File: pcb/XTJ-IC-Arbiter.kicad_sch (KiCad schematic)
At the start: 33 parts, among them J3 DTM13-12PA-R008, SW1 SW_DIP_x01, SW2 SW_DIP_x01, U1 LM2672N-5.0, U3 Teensy4.0, U4 MCP2562-H-P, U5 SP723ABG

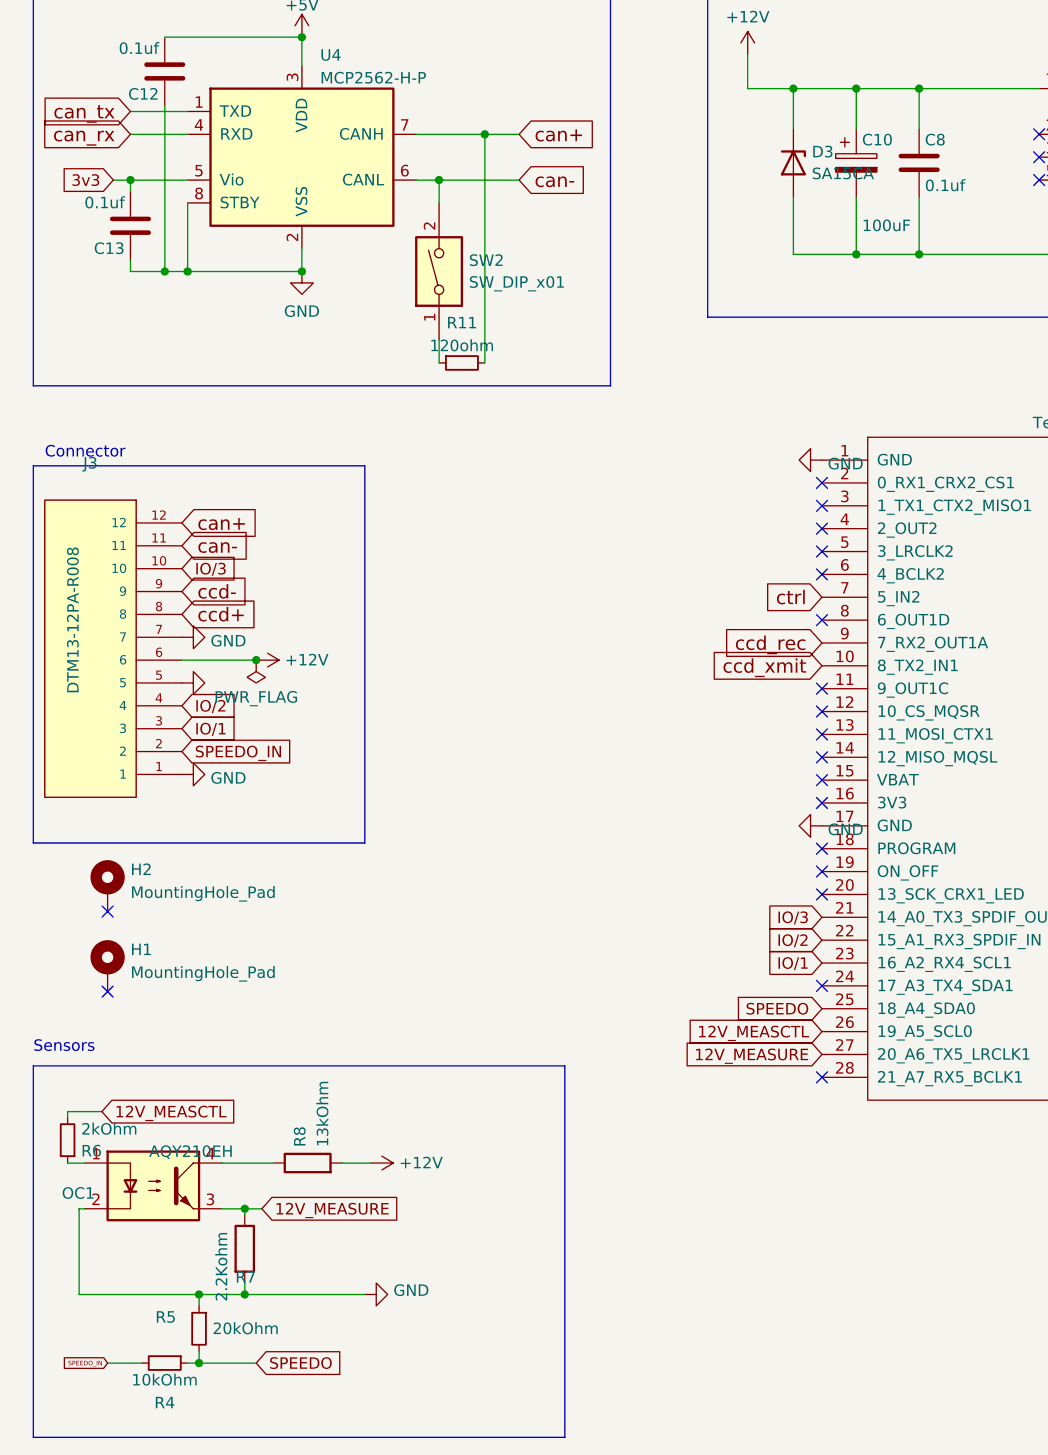
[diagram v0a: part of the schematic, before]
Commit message: Recalculate the 12v measure voltage dividers, and add a zener to limit to 3.3v
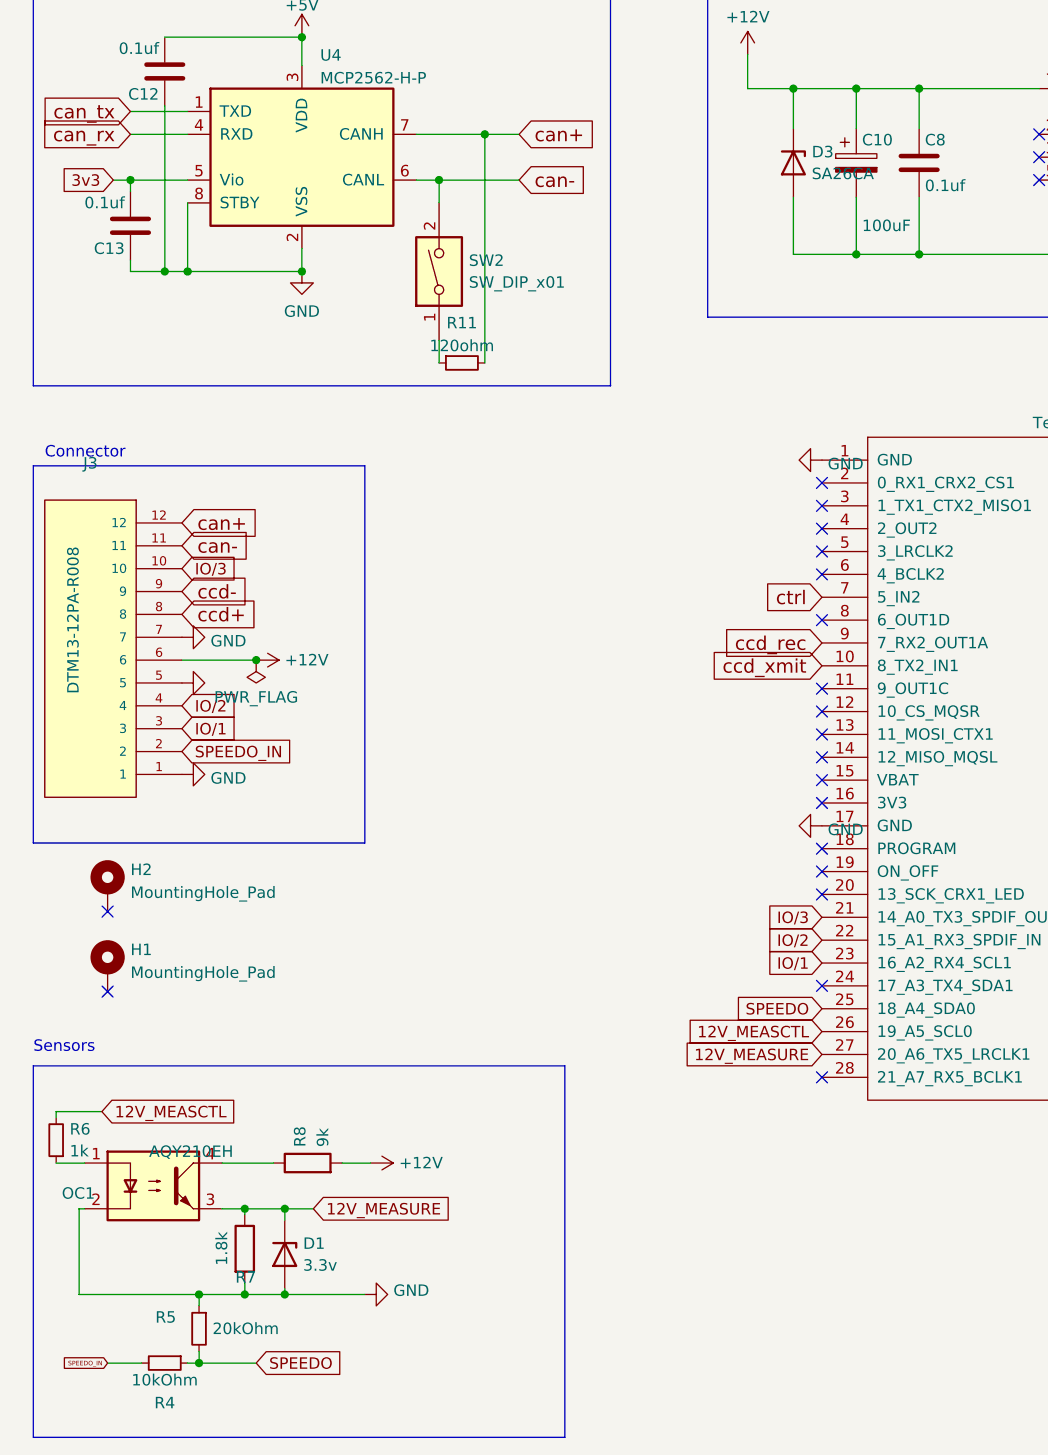
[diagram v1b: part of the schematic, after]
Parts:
- added D1: 3.3v, Diode_THT:D_DO-35_SOD27_P7.62mm_Horizontal, symbol Device:D_Zener
- D3: value SA15CA -> SA26CA
- R6: value 2kOhm -> 1k
- R7: value 2.2Kohm -> 1.8k
- R8: value 13kOhm -> 9k
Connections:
- net 12V_MEASURE: now also D1.1 (K)
- net GND: now also D1.2 (A)
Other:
- moved on the sheet: R6
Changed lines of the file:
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@@
   (junction (at 109.22 54.61) (diameter 0) (color 0 0 0 0)
   )
+  (junction (at 45.72 160.655) (diameter 0) (color 0 0 0 0)
+  )
   (junction (at 28.575 46.355) (diameter 0) (color 0 0 0 0)
   )
@@
   )
   (junction (at 62.865 46.355) (diameter 0) (color 0 0 0 0)
+  )
+  (junction (at 45.72 170.18) (diameter 0) (color 0 0 0 0)
   )
   (junction (at 249.555 34.29) (diameter 0) (color 0 0 0 0)
@@
     (stroke (width 0) (type default))
   )
+  (wire (pts (xy 45.72 169.545) (xy 45.72 170.18))
+    (stroke (width 0) (type default))
+  )
   (wire (pts (xy 161.29 135.89) (xy 167.005 135.89))
     (stroke (width 0) (type default))
@@
     (stroke (width 0) (type default))
   )
-  (wire (pts (xy 25.4 149.86) (xy 21.59 149.86))
+  (wire (pts (xy 25.4 149.86) (xy 20.32 149.86))
     (stroke (width 0) (type default))
   )
@@
     (stroke (width 0) (type default))
   )
-  (wire (pts (xy 21.59 155.575) (xy 23.495 155.575))
+  (wire (pts (xy 20.32 155.575) (xy 23.495 155.575))
     (stroke (width 0) (type default))
   )
@@
     (stroke (width 0) (type default))
   )
+  (wire (pts (xy 41.275 160.655) (xy 45.72 160.655))
+    (stroke (width 0) (type default))
+  )
   (wire (pts (xy 169.545 46.355) (xy 173.355 46.355))
     (stroke (width 0) (type default))
@@
     (stroke (width 0) (type default))
   )
-  (wire (pts (xy 43.18 160.655) (xy 41.275 160.655))
-    (stroke (width 0) (type default))
-  )
   (wire (pts (xy 207.645 34.29) (xy 207.645 57.785))
     (stroke (width 0) (type default))
@@
     (stroke (width 0) (type default))
   )
+  (wire (pts (xy 45.72 160.655) (xy 45.72 161.925))
+    (stroke (width 0) (type default))
+  )
   (wire (pts (xy 144.78 54.61) (xy 160.02 54.61))
     (stroke (width 0) (type default))
@@
     (stroke (width 0) (type default))
   )
+  (wire (pts (xy 45.72 170.18) (xy 54.61 170.18))
+    (stroke (width 0) (type default))
+  )
   (wire (pts (xy 109.22 36.195) (xy 116.205 36.195))
     (stroke (width 0) (type default))
   )
-  (wire (pts (xy 21.59 149.86) (xy 21.59 150.495))
+  (wire (pts (xy 20.32 149.86) (xy 20.32 150.495))
     (stroke (width 0) (type default))
   )
@@
     (stroke (width 0) (type default))
   )
+  (wire (pts (xy 45.72 160.655) (xy 48.895 160.655))
+    (stroke (width 0) (type default))
+  )
   (polyline (pts (xy 81.915 24.13) (xy 81.915 69.215))
     (stroke (width 0) (type default))
@@
     (stroke (width 0) (type default))
   )
-  (wire (pts (xy 41.275 170.18) (xy 54.61 170.18))
+  (wire (pts (xy 41.275 170.18) (xy 45.72 170.18))
     (stroke (width 0) (type default))
   )
@@
     )
   )
-  (global_label "12V_MEASURE" (shape input) (at 43.18 160.655 0) (fields_autoplaced)
+  (global_label "12V_MEASURE" (shape input) (at 48.895 160.655 0) (fields_autoplaced)
     (effects (font (size 1.27 1.27)) (justify left))
-    (property "Intersheetrefs" "${INTERSHEET_REFS}" (at 58.7164 160.7344 0)
+    (property "Intersheetrefs" "${INTERSHEET_REFS}" (at 64.4314 160.7344 0)
       (effects (font (size 1.27 1.27)) (justify left) hide)
     )
@@
       (effects (font (size 1.27 1.27)) (justify left))
     )
-    (property "Value" "13kOhm" (at 49.9622 153.797 0)
+    (property "Value" "9k" (at 49.9622 153.797 0)
       (effects (font (size 1.27 1.27)) (justify left))
     )
@@
     )
   )
-  (symbol (lib_id "Device:R_Small") (at 21.59 153.035 180) (unit 1)
-    (in_bom yes) (on_board yes) (dnp no) (fields_autoplaced)
-    (property "Reference" "R6" (at 23.0886 154.2471 0)
+  (symbol (lib_id "Device:R_Small") (at 20.32 153.035 180) (unit 1)
+    (in_bom yes) (on_board yes) (dnp no) (fields_autoplaced)
+    (property "Reference" "R6" (at 21.8186 151.8229 0)
       (effects (font (size 1.27 1.27)) (justify right))
     )
-    (property "Value" "2kOhm" (at 23.0886 151.8229 0)
+    (property "Value" "1k" (at 21.8186 154.2471 0)
       (effects (font (size 1.27 1.27)) (justify right))
     )
-    (property "Footprint" "Resistor_THT:R_Axial_DIN0207_L6.3mm_D2.5mm_P7.62mm_Horizontal" (at 21.59 153.035 0)
-      (effects (font (size 1.27 1.27)) hide)
-    )
-    (property "Datasheet" "~" (at 21.59 153.035 0)
+    (property "Footprint" "Resistor_THT:R_Axial_DIN0207_L6.3mm_D2.5mm_P7.62mm_Horizontal" (at 20.32 153.035 0)
+      (effects (font (size 1.27 1.27)) hide)
+    )
+    (property "Datasheet" "~" (at 20.32 153.035 0)
       (effects (font (size 1.27 1.27)) hide)
     )
@@
       (effects (font (size 1.27 1.27)) (justify right))
     )
-    (property "Value" "2.2Kohm" (at 38.735 163.195 90)
+    (property "Value" "1.8k" (at 38.735 163.195 90)
       (effects (font (size 1.27 1.27)) (justify right))
     )
@@
       (effects (font (size 1.27 1.27)) (justify left))
     )
-    (property "Value" "SA15CA" (at 104.267 45.6621 90)
+    (property "Value" "SA26CA" (at 104.267 45.6621 90)
       (effects (font (size 1.27 1.27)) (justify left))
     )
@@
         )
       )
+    )
+  )
+  (symbol (lib_id "Device:D_Zener") (at 45.72 165.735 270) (unit 1)
+    (in_bom yes) (on_board yes) (dnp no) (fields_autoplaced)
+    (property "Reference" "D1" (at 47.752 164.5229 90)
+      (effects (font (size 1.27 1.27)) (justify left))
+    )
+    (property "Value" "3.3v" (at 47.752 166.9471 90)
+      (effects (font (size 1.27 1.27)) (justify left))
+    )
+    (property "Footprint" "Diode_THT:D_DO-35_SOD27_P7.62mm_Horizontal" (at 45.72 165.735 0)
+      (effects (font (size 1.27 1.27)) hide)
+    )
+    (property "Datasheet" "~" (at 45.72 165.735 0)
+      (effects (font (size 1.27 1.27)) hide)
+    )
+    (pin "2")
+    (pin "1")
+    (instances
+      (project "XTJ-IC-Arbiter"
+        (path "/30a59342-dbf1-42d2-913c-7e79095896d9"
+          (reference "D1") (unit 1)
+        )
+      )

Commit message: ugly but functional
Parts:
- removed C2: 0.1uf, Capacitor_THT:C_Disc_D3.8mm_W2.6mm_P2.50mm, symbol Device:C
- added D2: 1N4001GH, Diode_THT:D_DO-41_SOD81_P7.62mm_Horizontal, symbol Device:D
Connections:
- net ctrl is gone; now on net ccd_rec: U2.13 (CTRL), U3.7 (5_IN2)
- net +5V: now also D2.2 (A)
- net 12V_MEASCTL: now also U3.27 (20_A6_TX5_LRCLK1); no longer U3.26 (19_A5_SCL0)
- net 12V_MEASURE: now also U3.26 (19_A5_SCL0); no longer U3.27 (20_A6_TX5_LRCLK1)
- net GND: no longer J3.5
- net IO/1: now also U5.7 (IN); no longer U5.5 (IN_4)
- net IO/3: now also U5.5 (IN_4); no longer U5.7 (IN)
- net can+: now also J3.9; no longer J3.12
- net can-: now also J3.8; no longer J3.11
- net ccd+: now also J3.11, U5.2 (IN_3); no longer J3.8, U5.1 (IN_2)
- net ccd-: now also J3.12, U5.1 (IN_2); no longer J3.9, U5.2 (IN_3)
- new net: D2.1 (K), J3.5

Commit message: less ugly
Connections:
- net 12V_MEASCTL: now also U3.24 (17_A3_TX4_SDA1); no longer U3.27 (20_A6_TX5_LRCLK1)
- net 12V_MEASURE: now also U3.25 (18_A4_SDA0); no longer U3.26 (19_A5_SCL0)
- net IO/1: now also J3.10, U3.21 (14_A0_TX3_SPDIF_OUT), U5.3 (IN_5); no longer J3.3, U3.23 (16_A2_RX4_SCL1), U5.7 (IN)
- net IO/2: now also J3.11, U3.23 (16_A2_RX4_SCL1), U5.2 (IN_3); no longer J3.4, U3.22 (15_A1_RX3_SPDIF_IN), U5.6 (IN_6)
- net IO/3: now also J3.12, U3.22 (15_A1_RX3_SPDIF_IN), U5.7 (IN); no longer J3.10, U3.21 (14_A0_TX3_SPDIF_OUT), U5.5 (IN_4)
- net SPEEDO: now also U3.26 (19_A5_SCL0), U5.1 (IN_2); no longer U3.25 (18_A4_SDA0), U5.3 (IN_5)
- net ccd+: now also J3.3, U5.6 (IN_6); no longer J3.11, U5.2 (IN_3)
- net ccd-: now also J3.4, U5.5 (IN_4); no longer J3.12, U5.1 (IN_2)
- net ccd_rec: now also U3.28 (21_A7_RX5_BCLK1); no longer U3.9 (7_RX2_OUT1A)
- net ccd_xmit: now also U3.27 (20_A6_TX5_LRCLK1); no longer U3.10 (8_TX2_IN1)

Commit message: polish, text
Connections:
- net IO/2: now also U3.22 (15_A1_RX3_SPDIF_IN), U5.7 (IN); no longer U3.23 (16_A2_RX4_SCL1), U5.2 (IN_3)
- net IO/3: now also U3.23 (16_A2_RX4_SCL1), U5.2 (IN_3); no longer U3.22 (15_A1_RX3_SPDIF_IN), U5.7 (IN)
- net ccd+: now also J3.4, U5.5 (IN_4); no longer J3.3, U5.6 (IN_6)
- net ccd-: now also J3.3, U5.6 (IN_6); no longer J3.4, U5.5 (IN_4)
- net 5VO: now reaches D2.1 (K), J3.5
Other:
- moved on the sheet: D2
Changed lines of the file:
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@@
+    (stroke (width 0) (type default))
+  )
+  (wire (pts (xy 45.085 102.235) (xy 34.29 102.235))
     (stroke (width 0) (type default))
   )
@@
     (stroke (width 0) (type default))
   )
-  (wire (pts (xy 41.91 102.235) (xy 42.545 102.235))
+  (wire (pts (xy 52.705 102.235) (xy 53.34 102.235))
     (stroke (width 0) (type default))
   )
@@
   )
   (text "Connector" (at 19.05 77.47 0)
+    (effects (font (size 1.27 1.27)) (justify left bottom))
+  )
+  (label "5VO" (at 45.085 102.235 0) (fields_autoplaced)
     (effects (font (size 1.27 1.27)) (justify left bottom))
   )
@@
     )
   )
-  (global_label "IO{slash}2" (shape input) (at 105.41 133.35 180) (fields_autoplaced)
+  (global_label "IO{slash}2" (shape input) (at 105.41 130.81 180) (fields_autoplaced)
     (effects (font (size 1.27 1.27)) (justify right))
-    (property "Intersheetrefs" "${INTERSHEET_REFS}" (at 98.5217 133.4294 0)
+    (property "Intersheetrefs" "${INTERSHEET_REFS}" (at 98.5217 130.8894 0)
       (effects (font (size 1.27 1.27)) (justify right) hide)
     )
@@
     )
   )
-  (global_label "ccd+" (shape input) (at 210.82 109.855 180) (fields_autoplaced)
+  (global_label "ccd+" (shape input) (at 210.82 104.775 180) (fields_autoplaced)
     (effects (font (size 1.524 1.524)) (justify right))
-    (property "Intersheetrefs" "${INTERSHEET_REFS}" (at 201.3599 109.855 0)
+    (property "Intersheetrefs" "${INTERSHEET_REFS}" (at 201.3599 104.775 0)
       (effects (font (size 1.27 1.27)) (justify right) hide)
     )
@@
     )
   )
-  (global_label "ccd+" (shape input) (at 34.29 107.315 0) (fields_autoplaced)
+  (global_label "ccd+" (shape input) (at 34.29 104.775 0) (fields_autoplaced)
     (effects (font (size 1.524 1.524)) (justify left))
-    (property "Intersheetrefs" "${INTERSHEET_REFS}" (at 256.54 212.725 0)
+    (property "Intersheetrefs" "${INTERSHEET_REFS}" (at 256.54 210.185 0)
       (effects (font (size 1.27 1.27)) hide)
     )
@@
     )
   )
-  (global_label "IO{slash}3" (shape input) (at 105.41 130.81 180) (fields_autoplaced)
+  (global_label "IO{slash}3" (shape input) (at 105.41 133.35 180) (fields_autoplaced)
     (effects (font (size 1.27 1.27)) (justify right))
-    (property "Intersheetrefs" "${INTERSHEET_REFS}" (at 98.5217 130.8894 0)
+    (property "Intersheetrefs" "${INTERSHEET_REFS}" (at 98.5217 133.4294 0)
       (effects (font (size 1.27 1.27)) (justify right) hide)
     )
@@
     )
   )
-  (global_label "IO{slash}3" (shape input) (at 210.82 112.395 180) (fields_autoplaced)
+  (global_label "IO{slash}3" (shape input) (at 210.82 102.235 180) (fields_autoplaced)
     (effects (font (size 1.27 1.27)) (justify right))
-    (property "Intersheetrefs" "${INTERSHEET_REFS}" (at 203.3595 112.395 0)
+    (property "Intersheetrefs" "${INTERSHEET_REFS}" (at 203.3595 102.235 0)
       (effects (font (size 1.27 1.27)) (justify right) hide)
     )
@@
     )
   )
-  (global_label "IO{slash}2" (shape input) (at 210.82 102.235 180) (fields_autoplaced)
+  (global_label "IO{slash}2" (shape input) (at 210.82 112.395 180) (fields_autoplaced)
     (effects (font (size 1.27 1.27)) (justify right))
-    (property "Intersheetrefs" "${INTERSHEET_REFS}" (at 203.3595 102.235 0)
+    (property "Intersheetrefs" "${INTERSHEET_REFS}" (at 203.3595 112.395 0)
       (effects (font (size 1.27 1.27)) (justify right) hide)
     )
@@
     )
   )
-  (global_label "ccd-" (shape input) (at 210.82 104.775 180) (fields_autoplaced)
+  (global_label "ccd-" (shape input) (at 210.82 109.855 180) (fields_autoplaced)
     (effects (font (size 1.524 1.524)) (justify right))
-    (property "Intersheetrefs" "${INTERSHEET_REFS}" (at 201.3599 104.775 0)
+    (property "Intersheetrefs" "${INTERSHEET_REFS}" (at 201.3599 109.855 0)
       (effects (font (size 1.27 1.27)) (justify right) hide)
     )
@@
     )
   )
-  (global_label "ccd-" (shape input) (at 34.29 104.775 0) (fields_autoplaced)
+  (global_label "ccd-" (shape input) (at 34.29 107.315 0) (fields_autoplaced)
     (effects (font (size 1.524 1.524)) (justify left))
-    (property "Intersheetrefs" "${INTERSHEET_REFS}" (at 260.35 241.935 0)
+    (property "Intersheetrefs" "${INTERSHEET_REFS}" (at 260.35 244.475 0)
       (effects (font (size 1.27 1.27)) hide)
     )
@@
     )
   )
-  (symbol (lib_id "power:+5V") (at 42.545 102.235 270) (unit 1)
-    (in_bom yes) (on_board yes) (dnp no) (fields_autoplaced)
-    (property "Reference" "#PWR012" (at 38.735 102.235 0)
-      (effects (font (size 1.27 1.27)) hide)
-    )
-    (property "Value" "+5V" (at 45.72 102.235 90)
-      (effects (font (size 1.27 1.27)) (justify left))
-    )
-    (property "Footprint" "" (at 42.545 102.235 0)
-      (effects (font (size 1.27 1.27)) hide)
-    )
-    (property "Datasheet" "" (at 42.545 102.235 0)
+  (symbol (lib_id "power:+5V") (at 53.34 102.235 180) (unit 1)
+    (in_bom yes) (on_board yes) (dnp no) (fields_autoplaced)
+    (property "Reference" "#PWR012" (at 53.34 98.425 0)
+      (effects (font (size 1.27 1.27)) hide)
+    )
+    (property "Value" "+5V" (at 53.34 106.3681 0)
+      (effects (font (size 1.27 1.27)))
+    )
+    (property "Footprint" "" (at 53.34 102.235 0)
+      (effects (font (size 1.27 1.27)) hide)
+    )
+    (property "Datasheet" "" (at 53.34 102.235 0)
       (effects (font (size 1.27 1.27)) hide)
     )
@@
     )
   )
-  (symbol (lib_id "Device:D") (at 38.1 102.235 0) (unit 1)
-    (in_bom yes) (on_board yes) (dnp no) (fields_autoplaced)
-    (property "Reference" "D2" (at 38.1 96.8207 0)
-      (effects (font (size 1.27 1.27)))
-    )
-    (property "Value" "1N4001GH " (at 38.1 99.2449 0)
-      (effects (font (size 1.27 1.27)))
-    )
-    (property "Footprint" "Diode_THT:D_DO-41_SOD81_P7.62mm_Horizontal" (at 38.1 102.235 0)
-      (effects (font (size 1.27 1.27)) hide)
-    )
-    (property "Datasheet" "~" (at 38.1 102.235 0)
-      (effects (font (size 1.27 1.27)) hide)
-    )
-    (property "Sim.Device" "D" (at 38.1 102.235 0)
-      (effects (font (size 1.27 1.27)) hide)
-    )
-    (property "Sim.Pins" "1=K 2=A" (at 38.1 102.235 0)
-      (effects (font (size 1.27 1.27)) hide)
-    )
+  (symbol (lib_id "Device:D") (at 48.895 102.235 0) (unit 1)
+    (in_bom yes) (on_board yes) (dnp no) (fields_autoplaced)
+    (property "Reference" "D2" (at 48.895 96.8207 0)
+      (effects (font (size 1.27 1.27)))
+    )
+    (property "Value" "1N4001GH " (at 48.895 99.2449 0)
+      (effects (font (size 1.27 1.27)))
+    )
+    (property "Footprint" "Diode_THT:D_DO-41_SOD81_P7.62mm_Horizontal" (at 48.895 102.235 0)
+      (effects (font (size 1.27 1.27)) hide)
+    )
+    (property "Datasheet" "~" (at 48.895 102.235 0)
+      (effects (font (size 1.27 1.27)) hide)
+    )
+    (property "Sim.Device" "D" (at 48.895 102.235 0)
+      (effects (font (size 1.27 1.27)) hide)
+    )
+    (property "Sim.Pins" "1=K 2=A" (at 48.895 102.235 0)
+      (effects (font (size 1.27 1.27)) hide)
+    )
